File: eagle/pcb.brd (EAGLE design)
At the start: 100 x 80 mm, 58 parts, among them J7 FEMALE 2x3, X1 16 MHz, X2 12 MHz

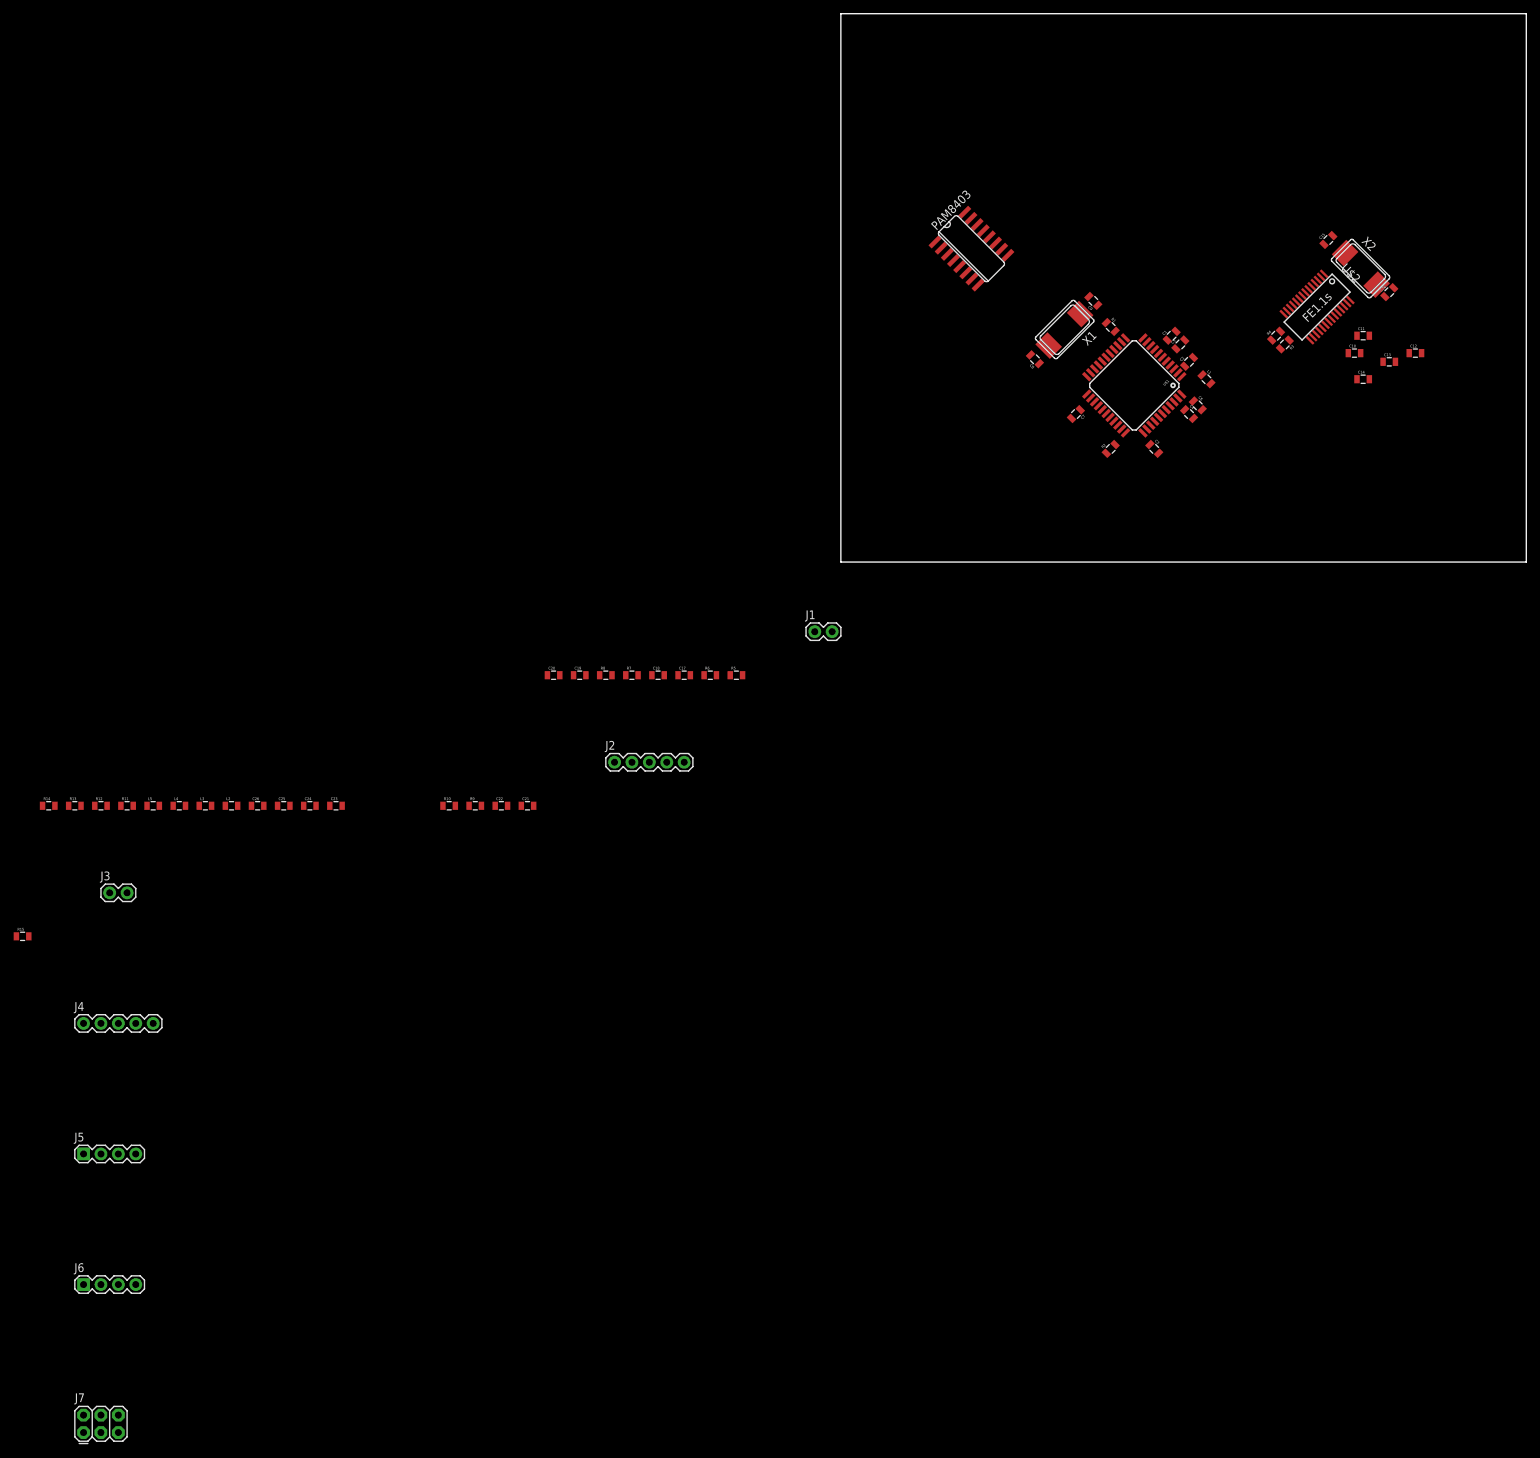
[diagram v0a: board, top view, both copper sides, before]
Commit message: top layer almost done, continue with bottom layer
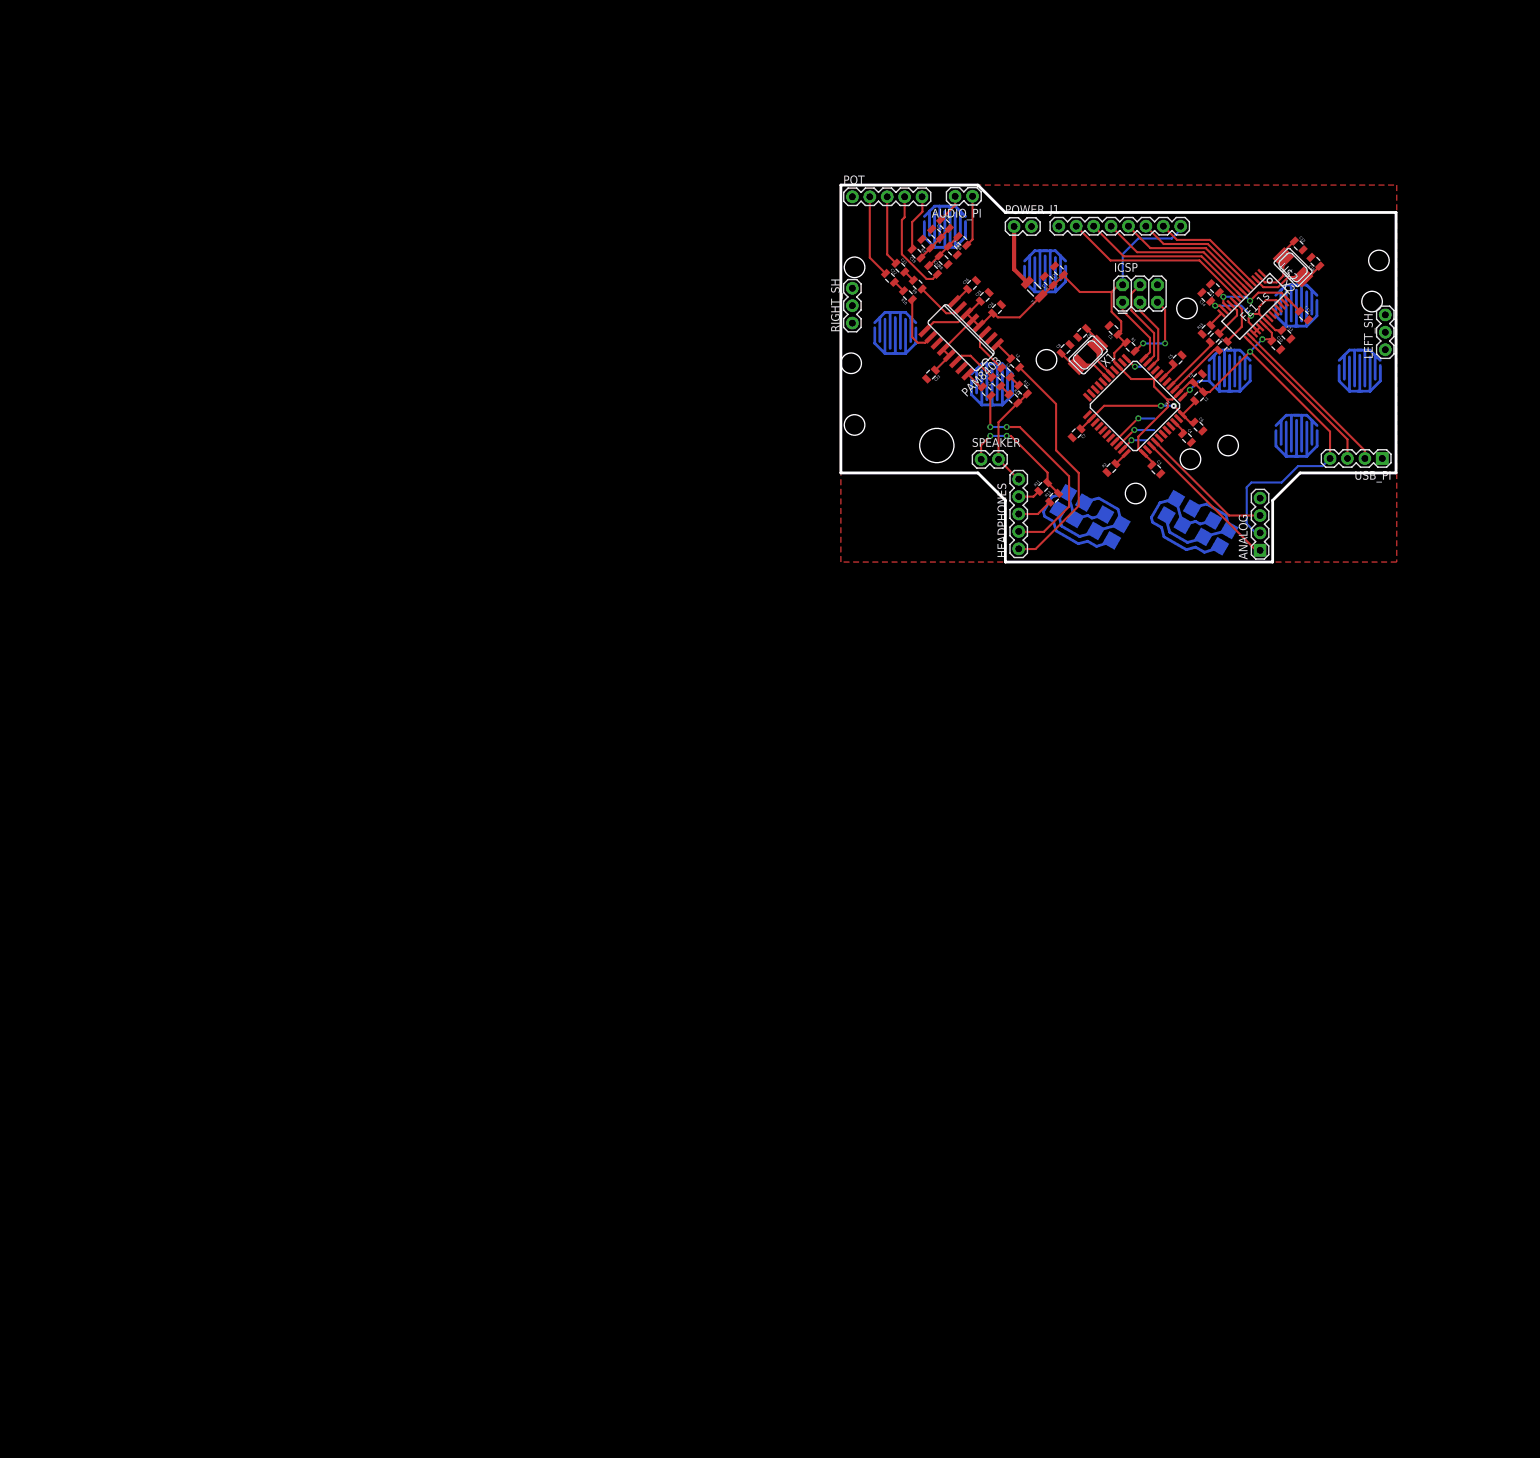
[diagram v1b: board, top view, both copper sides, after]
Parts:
- removed J2, J4: (no value), SparkFun-Connectors:1X05
- removed J3: (no value), SparkFun-Connectors:1X02
- removed J5, J6: (no value), SparkFun-Connectors:1X04
- removed J7: FEMALE 2x3, SparkFun-Connectors:2X3
- added A, B, DOWN, LEFT, RIGHT, UP, X, Y: (no value), dmg-conductive:CIRCLE_BUTTON2
- added ANALOG, USB_PI: (no value), SparkFun-Connectors:1X04
- added AUDIO_PI, POWER, SPEAKER: (no value), SparkFun-Connectors:1X02
- added C27: 1u, SparkFun-Passives:0805
- added C28: 10u, SparkFun-Passives:0805
- added F1: PTCSMD, SparkFun-PowerIC:PTC-1206
- added HEADPHONES, POT: (no value), SparkFun-Connectors:1X05
- added ICSP: FEMALE 2x3, SparkFun-Connectors:2X3
- added LEFT_SH, RIGHT_SH: (no value), SparkFun-Connectors:1X03
- added SELECT, START: (no value), dmg-conductive:START_STOP2
- J1: device SparkFun-Connectors:1X02 -> SparkFun-Connectors:1X08_ROUND
- X1, X2: device adafruit:NX8045 -> adafruit:NX5032
- moved R15 194.1 mm to (53.4, 33.9), turned to 45 degrees
- moved R14 152.8 mm to (25.2, 23.8), turned to 315 degrees
- moved R13 149.8 mm to (31.1, 9.38), turned to 45 degrees
- moved R12 147.6 mm to (26.6, 25.2), turned to 315 degrees
- moved R11 141.5 mm to (29.5, 11.0), turned to 45 degrees
- moved L5 137.7 mm to (22.7, 26.3), turned to 315 degrees
- moved L3 132.8 mm to (24.1, 27.7), turned to 315 degrees
- moved L4 132.4 mm to (21.3, 24.9), turned to 315 degrees
- moved L2 131.3 mm to (25.4, 29.0), turned to 315 degrees
- moved C26 129.0 mm to (19.1, 40.4), turned to 45 degrees
- moved C25 126.4 mm to (21.0, 38.7), turned to 45 degrees
- moved C24 123.7 mm to (22.8, 36.9), turned to 45 degrees
- moved C23 107.2 mm to (13.1, 27.4), turned to 225 degrees
- moved R10 100.1 mm to (9.78, 38.9), turned to 135 degrees
- moved R9 99.7 mm to (11.2, 40.5), turned to 135 degrees
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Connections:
- removed net N$1: R1.2, U$1.13
- removed net N$27: J4.1, L2.2
- removed net N$31: J4.2, L4.2
- removed net N$38: J3.1, R11.2, R13.2
- new net A: A.1, U$1.27
- new net AUDIO_GND: HEADPHONES.5, R12.2, R14.2, SPEAKER.2
- new net AUDIO_L2MONO: HEADPHONES.4, R11.1
- new net AUDIO_MONO: R11.2, R13.2, SPEAKER.1
- new net AUDIO_R2MONO: HEADPHONES.3, R13.1
- new net AUDIO_STEREO_L: HEADPHONES.1, L2.2
- new net AUDIO_STEREO_R: HEADPHONES.2, L4.2
- new net B: B.1, U$1.26
- new net DOWN: DOWN.1, U$1.32
- new net L1: LEFT_SH.1, U$1.30
- new net L2: LEFT_SH.3, U$1.20
- new net LEFT: LEFT.1, U$1.31
- new net MISO: ICSP.1, U$1.11
- new net MOSI: ICSP.4, U$1.10
- new net N$34: J1.7, U$2.4
- new net N$40: J1.3, U$2.8
- new net N$43: J1.2, U$2.9
- new net N$50: F1.2, POWER.1
- new net R1: RIGHT_SH.1, U$1.25
- new net R2: RIGHT_SH.3, U$1.21
- new net RESET: ICSP.5, R1.2, U$1.13
- new net RIGHT: RIGHT.1, U$1.1
- new net SCK: ICSP.3, U$1.9
- new net SELECT: SELECT.1, U$1.28
- new net START: START.1, U$1.29
- new net UP: U$1.12, UP.1
- new net X: U$1.19, X.1
- new net Y: U$1.18, Y.1
- net GND: now also A.2, ANALOG.4, B.2, C27.2, C28.2, DOWN.2, ICSP.6, J1.1, LEFT.2, LEFT_SH.2, POT.1, POWER.2, RIGHT.2, RIGHT_SH.2, SELECT.2, START.2, UP.2, USB_PI.1, X.2, Y.2; no longer J2.1, J5.4, J6.1
- net N$13: now also AUDIO_PI.2; no longer J1.2
- net N$14: now also AUDIO_PI.1; no longer J1.1
- net N$19: now also POT.5; no longer J2.5
- net N$20: now also POT.4; no longer J2.4
- net N$21: now also POT.3; no longer J2.3
- net N$22: now also POT.2; no longer J2.2
- net N$35: now also J1.6, U$2.5; no longer J4.3, R13.1
- net N$36: now also J1.5, U$2.6; no longer J4.4, R11.1
- net N$39: now also J1.4, U$2.7; no longer J3.2, J4.5, R12.2, R14.2
- net N$41: now also ANALOG.1; no longer J5.1
- net N$42: now also ANALOG.3; no longer J5.3
- net N$45: now also USB_PI.3; no longer J6.3
- net N$46: now also USB_PI.2; no longer J6.2
- net VCC: now also ANALOG.2, C27.1, C28.1, F1.1, ICSP.2, J1.8, USB_PI.4; no longer J5.2, J6.4
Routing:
- net VCC: track 0.00 -> 166.8 mm, vias 0 -> 2
- net AUDIO_STEREO_L: track 0.00 -> 35.1 mm
- net AUDIO_STEREO_R: track 0.00 -> 32.4 mm, vias 0 -> 2
- net N$43: track 0.00 -> 27.8 mm
- net N$40: track 0.00 -> 25.5 mm
- net N$46: track 0.00 -> 24.7 mm
- net N$45: track 0.00 -> 23.4 mm
- net N$39: track 0.00 -> 23.2 mm
- net 3.3V: track 0.00 -> 23.2 mm, vias 0 -> 2
- net N$41: track 0.00 -> 22.2 mm
- net VCCA: track 0.00 -> 22.1 mm, vias 0 -> 2
- net N$36: track 0.00 -> 21.0 mm
- net N$42: track 0.00 -> 19.7 mm
- net N$35: track 0.00 -> 18.7 mm
- net AUDIO_MONO: track 0.00 -> 18.2 mm, vias 0 -> 2
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- added copper zone on layer 1, net GND
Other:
- board size 100 x 80 mm -> 81 x 55 mm

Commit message: completed routing top and bottom
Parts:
- moved POWER 59.5 mm to (73.9, 14.6), turned to 180 degrees
- moved F1 38.7 mm to (63.9, 24.7), turned to 315 degrees
- moved C28 36.0 mm to (61.6, 23.3), turned to 315 degrees
- moved C27 35.0 mm to (59.8, 21.5), turned to 315 degrees
- moved USB_PI 7.17 mm to (79.3, 22.3), turned to 270 degrees
- moved J1 6.49 mm to (25.3, 49.4)
- moved SPEAKER 3.26 mm to (17.2, 14.6)
- moved RIGHT_SH 3.13 mm to (1.62, 31.7)
- moved ICSP 2.70 mm to (38.9, 39.4)
- moved R1 2.30 mm to (42.4, 33.7)
- moved START 0.90 mm to (52.1, 6.64)
- moved L1 0.64 mm to (52.8, 23.8)
- moved C7 0.57 mm to (34.0, 19.2)
- moved C1 0.45 mm to (39.6, 33.5)
- moved HEADPHONES 0.40 mm to (25.7, 1.66)
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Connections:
- removed net N$50: F1.2, POWER.1
- new net VCC_POWER: F1.2, POWER.1, USB_PI.4
- net VCC: no longer USB_PI.4
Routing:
- net R1: track 0.00 -> 53.2 mm, vias 0 -> 1
- net L2: track 0.00 -> 47.4 mm, vias 0 -> 1
- net R2: track 0.00 -> 46.3 mm, vias 0 -> 1
- net L1: track 7.20 -> 46.5 mm
- net A: track 0.00 -> 34.2 mm, vias 0 -> 1
- net X: track 0.00 -> 32.1 mm, vias 0 -> 1
- net START: track 0.00 -> 30.4 mm, vias 0 -> 1
- net LEFT: track 6.19 -> 36.1 mm
- net B: track 0.00 -> 26.1 mm, vias 0 -> 1
- net DOWN: track 4.18 -> 29.8 mm
- net Y: track 0.00 -> 21.9 mm, vias 0 -> 1
- net UP: track 2.77 -> 24.4 mm
- net SELECT: track 0.00 -> 20.5 mm, vias 0 -> 1
- net VCC_POWER: track 0.00 -> 18.3 mm
- net VCC: track 166.8 -> 149.5 mm, vias 2 -> 3
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- added copper zone on layer 16, net GND

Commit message: finished v0.2 and gerber files
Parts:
- removed J1: (no value), SparkFun-Connectors:1X08_ROUND
- added USB_HUB: (no value), SparkFun-Connectors:1X08_ROUND
- C17, C18: value 100n -> 33n
- C19, C20: value 100n -> 10u
- C21, C22: value 100n -> 220n
- C26: value 100n -> 1u
- R11, R12, R13, R14: value 10k -> 100
- R15: value 10k -> 2.7k
- R3, R4: value 10k -> 22
- R5, R6: value 10k -> 270
- R7, R8: value 10k -> 150
- moved HEADPHONES 25.8 mm to (51.4, 1.61), turned to 180 degrees
- moved SPEAKER 16.1 mm to (26.7, 1.65), turned to 90 degrees
- moved R11 8.92 mm to (33.4, 2.92), turned to 225 degrees
- moved R13 5.02 mm to (31.8, 4.41), turned to 225 degrees
- moved C8 1.30 mm to (32.7, 32.4)
- moved C9 1.22 mm to (35.0, 34.6)
- moved X1 1.20 mm to (35.9, 31.4)
- moved C1 1.10 mm to (39.7, 34.6)
- moved R4 1.00 mm to (55.7, 32.6)
- moved RIGHT_SH 1.00 mm to (1.62, 32.7)
- moved AUDIO_PI 1.00 mm to (19.2, 54.4)
- moved B 1.00 mm to (22.1, 26.9)
- moved C10 1.00 mm to (63.5, 32.6)
- moved C11 1.00 mm to (54.6, 41.0)
- moved C12 1.00 mm to (67.6, 37.0)
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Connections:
- net GND: now also USB_HUB.1; no longer J1.1
- net N$34: now also USB_HUB.7; no longer J1.7
- net N$35: now also USB_HUB.6; no longer J1.6
- net N$36: now also USB_HUB.5; no longer J1.5
- net N$39: now also USB_HUB.4; no longer J1.4
- net N$40: now also USB_HUB.3; no longer J1.3
- net N$43: now also USB_HUB.2; no longer J1.2
- net VCC: now also USB_HUB.8; no longer J1.8
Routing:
- net AUDIO_GND: track 18.9 -> 39.2 mm, vias 0 -> 1
- net AUDIO_MONO: track 20.4 -> 8.15 mm, vias 2 -> 0
- net AUDIO_STEREO_R: track 32.7 -> 43.3 mm, vias 2 -> 0
- net AUDIO_R2MONO: track 5.65 -> 16.1 mm
- net AUDIO_STEREO_L: track 35.5 -> 45.4 mm
- net AUDIO_L2MONO: track 3.66 -> 11.5 mm
- net RESET: track 19.0 -> 14.4 mm, vias 2 -> 1
- net GND: track 13.0 -> 10.7 mm
- net VCC: track 149.5 -> 151.1 mm
- net SELECT: track 20.5 -> 22.0 mm
- net A: track 34.2 -> 33.5 mm
- net START: track 30.4 -> 31.1 mm
- net R1: track 53.2 -> 52.6 mm
- net N$41: track 22.4 -> 23.0 mm
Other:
- board size 81 x 55 mm -> 81 x 56 mm
- board text added: "DMG Zero v0.2 jctots 2016"
- board text added: "GND"
- board text added: "MISO"
- board text added: "MOSI"
- board text added: "RESET"
- board text added: "SCK"
- board text added: "VCC"

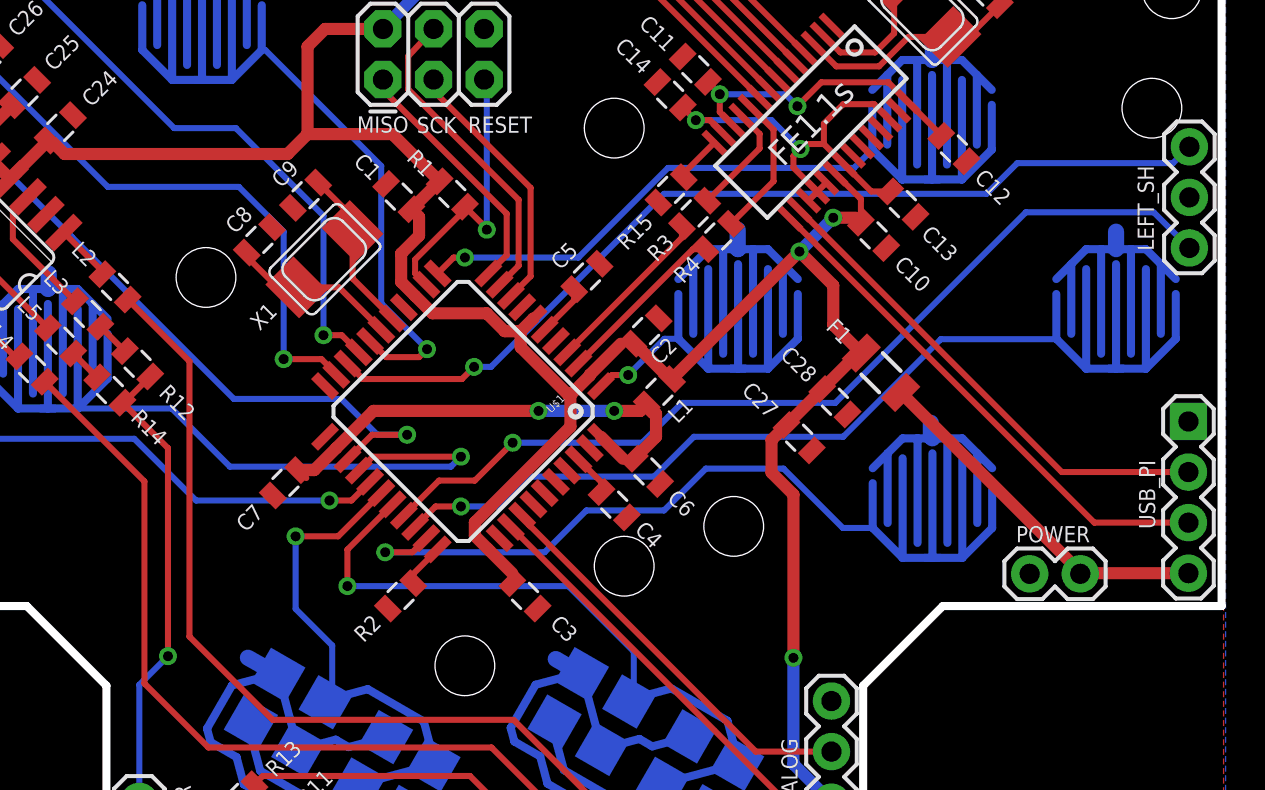
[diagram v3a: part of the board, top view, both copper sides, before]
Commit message: v0.3, moved the left shoulder away from rpi zero
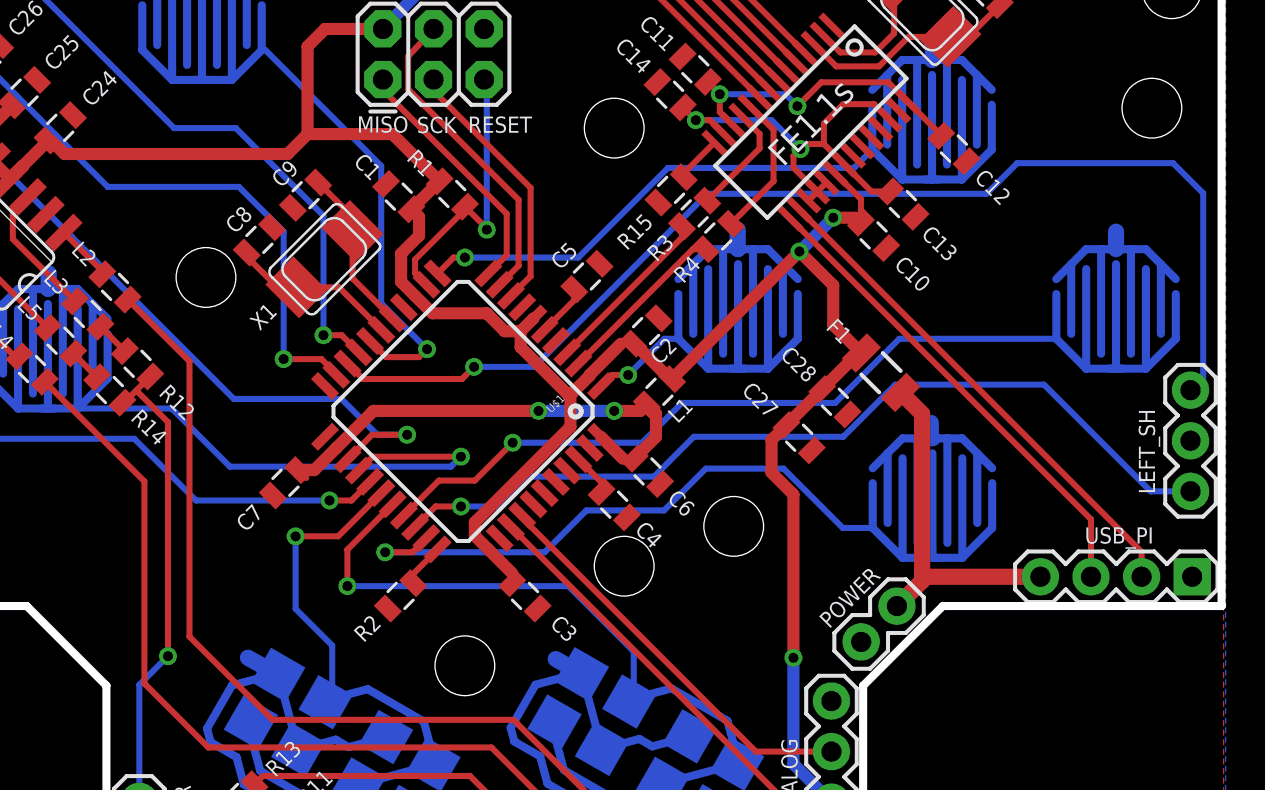
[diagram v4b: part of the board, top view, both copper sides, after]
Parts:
- moved LEFT_SH 12.2 mm to (79.4, 19.8)
- moved POWER 9.35 mm to (64.7, 14.0), turned to 225 degrees
- moved USB_PI 7.80 mm to (79.5, 15.5), turned to 180 degrees
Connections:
- net L1: now also U$1.31; no longer U$1.30
- net LEFT: now also U$1.30; no longer U$1.31
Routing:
- net L2: track 47.4 -> 58.6 mm
- net L1: track 46.5 -> 44.1 mm
- net N$45: track 26.3 -> 24.2 mm
- net VCC_POWER: track 18.3 -> 17.7 mm
- net N$46: track 25.0 -> 25.6 mm
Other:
- board text added: "DMG Zero v0.3 jctots 2016"
- board text removed: "DMG Zero v0.2 jctots 2016"
